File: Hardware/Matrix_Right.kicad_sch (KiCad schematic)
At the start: 0 parts

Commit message: Schematic review
Initial shcematic iteration.
Added all footprints and part numbers.
Only a quick review was performed.
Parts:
- added C48, C49, C50, C51, C52, C53, C54, C55, C56, C57, C58, C59, C60, C61, C62, C63, C64, C65, C66, C67, C68, C69, C70, C71, C72, C73, C74, C75, C76, C77, C78, C79, C80, C81, C82: 1u, Capacitor_SMD:C_0603_1608Metric, symbol Device:C
- added D100, D101, D107, D108, D109, D110, D111, D117, D118, D120, D121, D122, D127, D128, D130, D131, D132, D137, D138, D139, D140, D141, D77, D78, D79, D80, D81, D87, D88, D89, D90, D91, D97, D98, D99: SK6812MINI-E, LED_SMD:LED_SK6812MINI-E_3.2x2.8mm_P1.5mm_ReverseMount, symbol LED:SK6812MINI-E
- added D102, D103, D104, D105, D106, D112, D113, D114, D115, D116, D119, D123, D124, D125, D126, D129, D133, D134, D135, D136, D142, D143, D144, D145, D146, D82, D83, D84, D85, D86, D92, D93, D94, D95, D96: 1N4148WT, Diode_SMD:D_SOD-523, symbol Diode:1N4148WT
- added SW36, SW37, SW38, SW39, SW40, SW41, SW42, SW43, SW44, SW45, SW46, SW47, SW48, SW49, SW50, SW51, SW52, SW53, SW54, SW55, SW56, SW57, SW58, SW59, SW60, SW61, SW62, SW63, SW64, SW65, SW66, SW67: PG1350, Custom_Parts:PG1350_1.00u_PCB, symbol Switch:SW_Push
- added SW68: ENCODER, Custom_Parts:ALPS_EC11J_ENCODER, symbol Device:RotaryEncoder_Switch_MP
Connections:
- new net: D124.2 (A), SW57.2
- new net: D135.2 (A), SW62.2
- new net: D125.2 (A), SW58.2
- new net: D84.2 (A), SW38.2
- new net: D113.2 (A), SW52.2
- new net: D80.4 (DOUT), D90.2 (DIN)
- new net: D100.2 (DIN), D90.4 (DOUT)
- new net: D122.4 (DOUT), D132.2 (DIN)
- new net: D132.4 (DOUT), D141.2 (DIN)
- new net: D86.2 (A), SW40.2
- new net: D78.2 (DIN), D88.4 (DOUT)
- new net: D78.4 (DOUT), D81.2 (DIN)
- new net: D106.2 (A), SW50.2
- new net: D144.2 (A), SW66.2
- new net: D100.4 (DOUT), D110.2 (DIN)
- new net: D110.4 (DOUT), D121.2 (DIN)
- new net: D142.2 (A), SW64.2
- new net: D131.4 (DOUT), D140.2 (DIN)
- new net: D138.2 (DIN), D140.4 (DOUT)
- new net: D93.2 (A), SW42.2
- new net: D107.2 (DIN), D117.4 (DOUT)
- new net: D107.4 (DOUT), D97.2 (DIN)
- new net: D88.2 (DIN), D98.4 (DOUT)
- new net: D136.2 (A), SW63.2
- new net: D96.2 (A), SW45.2
- new net: D134.2 (A), SW61.2
- new net: D109.4 (DOUT), D120.2 (DIN)
- new net: D120.4 (DOUT), D130.2 (DIN)
- new net: D83.2 (A), SW37.2
- new net: D114.2 (A), SW53.2
- new net: D123.2 (A), SW56.2
- new net: D116.2 (A), SW55.2
- new net: D143.2 (A), SW65.2
- new net: D108.4 (DOUT), D98.2 (DIN)
- new net: D101.2 (DIN), D91.4 (DOUT)
- new net: D101.4 (DOUT), D111.2 (DIN)
- new net: D89.4 (DOUT), D99.2 (DIN)
- new net: D109.2 (DIN), D99.4 (DOUT)
- new net: D95.2 (A), SW44.2
- new net: D111.4 (DOUT), D122.2 (DIN)
- new net: D127.2 (DIN), D137.4 (DOUT)
- new net: D117.2 (DIN), D127.4 (DOUT)
- new net: D121.4 (DOUT), D131.2 (DIN)
- new net: D82.2 (A), SW36.2
- new net: D130.4 (DOUT), D139.2 (DIN)
- new net: D104.2 (A), SW48.2
- new net: D105.2 (A), SW49.2
- new net: D145.2 (A), SW67.2
- new net: D126.2 (A), SW59.2
- new net: D103.2 (A), SW47.2
- new net: D128.2 (DIN), D138.4 (DOUT)
- new net: D118.2 (DIN), D128.4 (DOUT)
- new net: D108.2 (DIN), D118.4 (DOUT)
- new net: D102.2 (A), SW46.2
- new net: D77.2 (DIN), D87.4 (DOUT)
- new net: D77.4 (DOUT), D80.2 (DIN)
- new net: D81.4 (DOUT), D91.2 (DIN)
- new net: D85.2 (A), SW39.2
- new net: D94.2 (A), SW43.2
- new net: D133.2 (A), SW60.2
- new net: D115.2 (A), SW54.2
- new net: D87.2 (DIN), D97.4 (DOUT)
- new net: D112.2 (A), SW51.2
- new net: D79.4 (DOUT), D89.2 (DIN)
- new net: D137.2 (DIN), D139.4 (DOUT)
- new net: D92.2 (A), SW41.2
- new net 5VR: C48.1, C49.1, C50.1, C51.1, C52.1, C53.1, C54.1, C55.1, C56.1, C57.1, C58.1, C59.1, C60.1, C61.1, C62.1, C63.1, C64.1, C65.1, C66.1, C67.1, C68.1, C69.1, C70.1, C71.1, C72.1, C73.1, C74.1, C75.1, C76.1, C77.1, C78.1, C79.1, C80.1, C81.1, C82.1, D100.3 (VDD), D101.3 (VDD), D107.3 (VDD), D108.3 (VDD), D109.3 (VDD), D110.3 (VDD), D111.3 (VDD), D117.3 (VDD), D118.3 (VDD), D120.3 (VDD), D121.3 (VDD), D122.3 (VDD), D127.3 (VDD), D128.3 (VDD), D130.3 (VDD), D131.3 (VDD), D132.3 (VDD), D137.3 (VDD), D138.3 (VDD), D139.3 (VDD), D140.3 (VDD), D141.3 (VDD), D77.3 (VDD), D78.3 (VDD), D79.3 (VDD), D80.3 (VDD), D81.3 (VDD), D87.3 (VDD), D88.3 (VDD), D89.3 (VDD), D90.3 (VDD), D91.3 (VDD), D97.3 (VDD), D98.3 (VDD), D99.3 (VDD)
- new net COL1_R: SW36.1, SW37.1, SW38.1, SW39.1, SW40.1
- new net COL2_R: SW41.1, SW42.1, SW43.1, SW44.1, SW45.1
- new net COL3_R: SW46.1, SW47.1, SW48.1, SW49.1, SW50.1
- new net COL4_R: SW51.1, SW52.1, SW53.1, SW54.1, SW55.1
- new net COL5_R: D119.2 (A), SW56.1, SW57.1, SW58.1, SW59.1
- new net COL6_R: D129.2 (A), SW60.1, SW61.1, SW62.1, SW63.1
- new net COL7_R: SW64.1, SW65.1, SW66.1, SW67.1, SW68.S1
- new net ENC_CC: D129.1 (K), SW68.B
- new net ENC_CW: D119.1 (K), SW68.A
- new net ENC_SW: D146.2 (A), SW68.S2
- new net GND: C48.2, C49.2, C50.2, C51.2, C52.2, C53.2, C54.2, C55.2, C56.2, C57.2, C58.2, C59.2, C60.2, C61.2, C62.2, C63.2, C64.2, C65.2, C66.2, C67.2, C68.2, C69.2, C70.2, C71.2, C72.2, C73.2, C74.2, C75.2, C76.2, C77.2, C78.2, C79.2, C80.2, C81.2, C82.2, D100.1 (VSS), D101.1 (VSS), D107.1 (VSS), D108.1 (VSS), D109.1 (VSS), D110.1 (VSS), D111.1 (VSS), D117.1 (VSS), D118.1 (VSS), D120.1 (VSS), D121.1 (VSS), D122.1 (VSS), D127.1 (VSS), D128.1 (VSS), D130.1 (VSS), D131.1 (VSS), D132.1 (VSS), D137.1 (VSS), D138.1 (VSS), D139.1 (VSS), D140.1 (VSS), D141.1 (VSS), D77.1 (VSS), D78.1 (VSS), D79.1 (VSS), D80.1 (VSS), D81.1 (VSS), D87.1 (VSS), D88.1 (VSS), D89.1 (VSS), D90.1 (VSS), D91.1 (VSS), D97.1 (VSS), D98.1 (VSS), D99.1 (VSS), SW68.MP
- new net LED_DATA_R: D79.2 (DIN)
- new net ROW1_R: D102.1 (K), D112.1 (K), D123.1 (K), D133.1 (K), D142.1 (K), D82.1 (K), D92.1 (K)
- new net ROW2_R: D103.1 (K), D113.1 (K), D124.1 (K), D134.1 (K), D143.1 (K), D83.1 (K), D93.1 (K)
- new net ROW3_R: D104.1 (K), D114.1 (K), D125.1 (K), D135.1 (K), D144.1 (K), D84.1 (K), D94.1 (K)
- new net ROW4_R: D105.1 (K), D115.1 (K), D126.1 (K), D136.1 (K), D145.1 (K), D85.1 (K), D95.1 (K)
- new net ROW5_R: D106.1 (K), D116.1 (K), D146.1 (K), D86.1 (K), D96.1 (K), SW68.C
- no-connect marks 0 -> 1

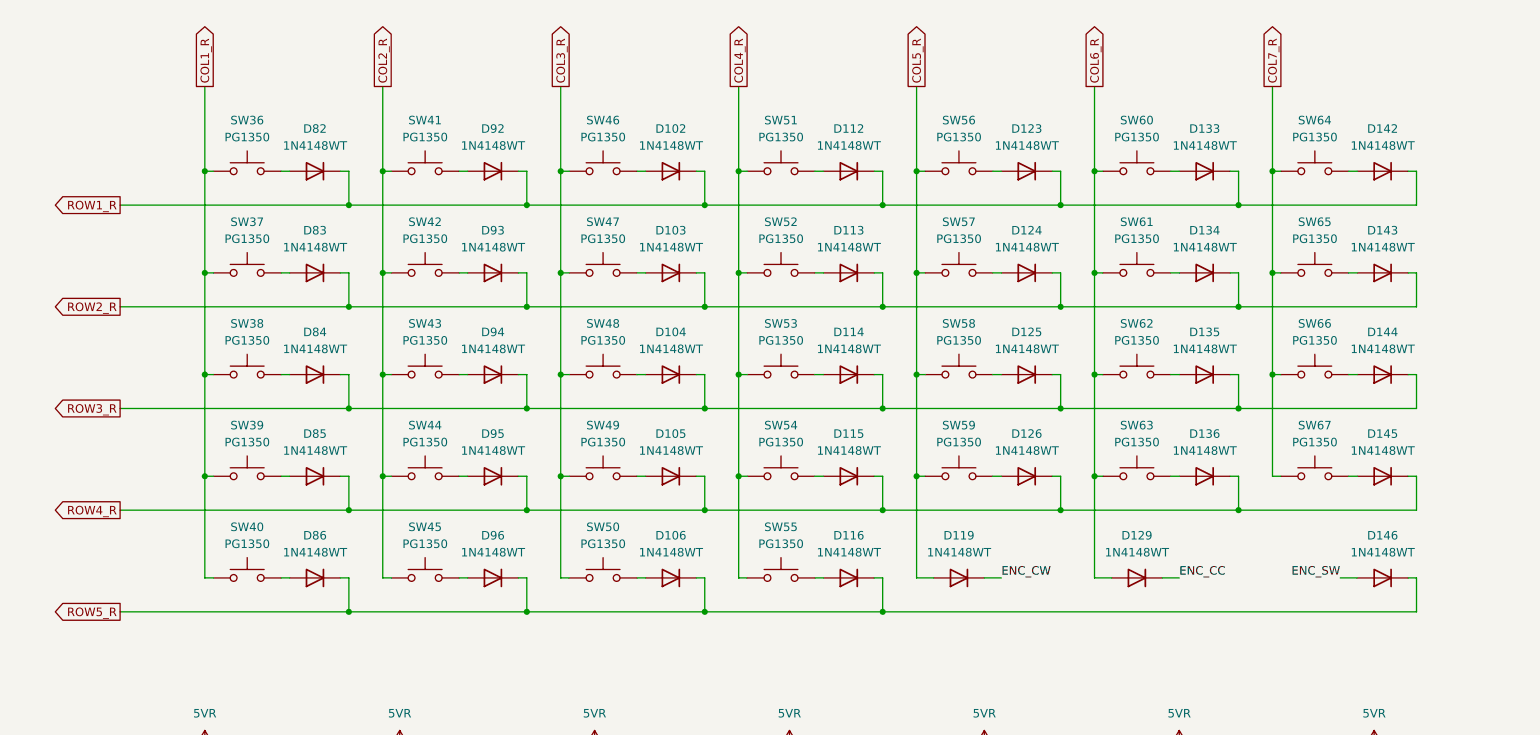
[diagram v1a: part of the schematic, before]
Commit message: Net configurations
Added net labels.
Updated the PCB components.
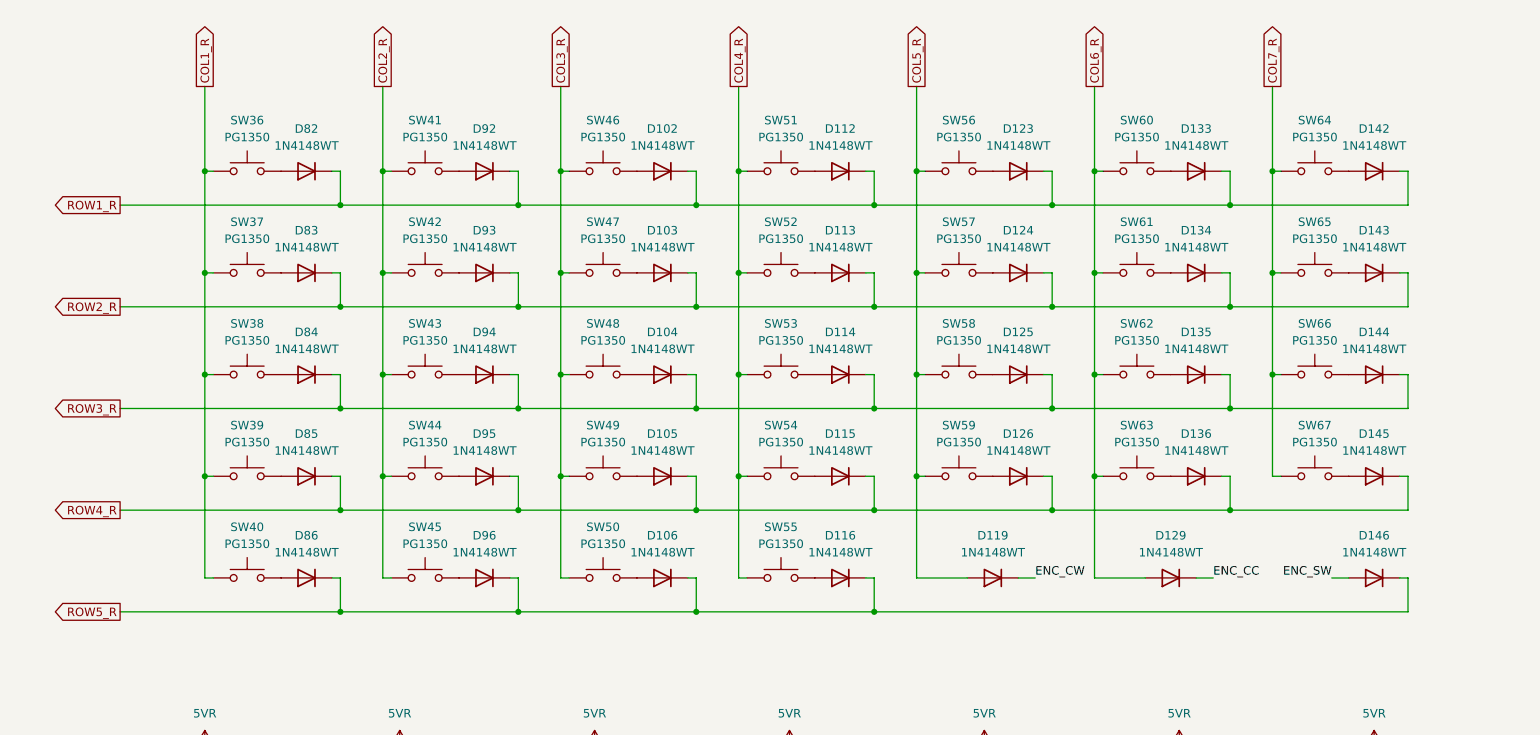
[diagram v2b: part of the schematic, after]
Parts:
- D100, D101, D107, D108, D109, D110, D111, D117, D118, D120, D121, D122, D127, D128, D130, D131, D132, D137, D138, D139, D140, D141, D77, D78, D79, D80, D81, D87, D88, D89, D90, D91, D97, D98, D99: footprint LED_SMD:LED_SK6812MINI-E_3.2x2.8mm_P1.5mm_ReverseMount -> Custom_Parts:LED_SK6812MINI-E_3.2x2.8mm_P1.5mm_ReverseMount
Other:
- moved on the sheet: D102, D103, D104, D105, D106, D112, D113, D114, D115, D116, D119, D123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

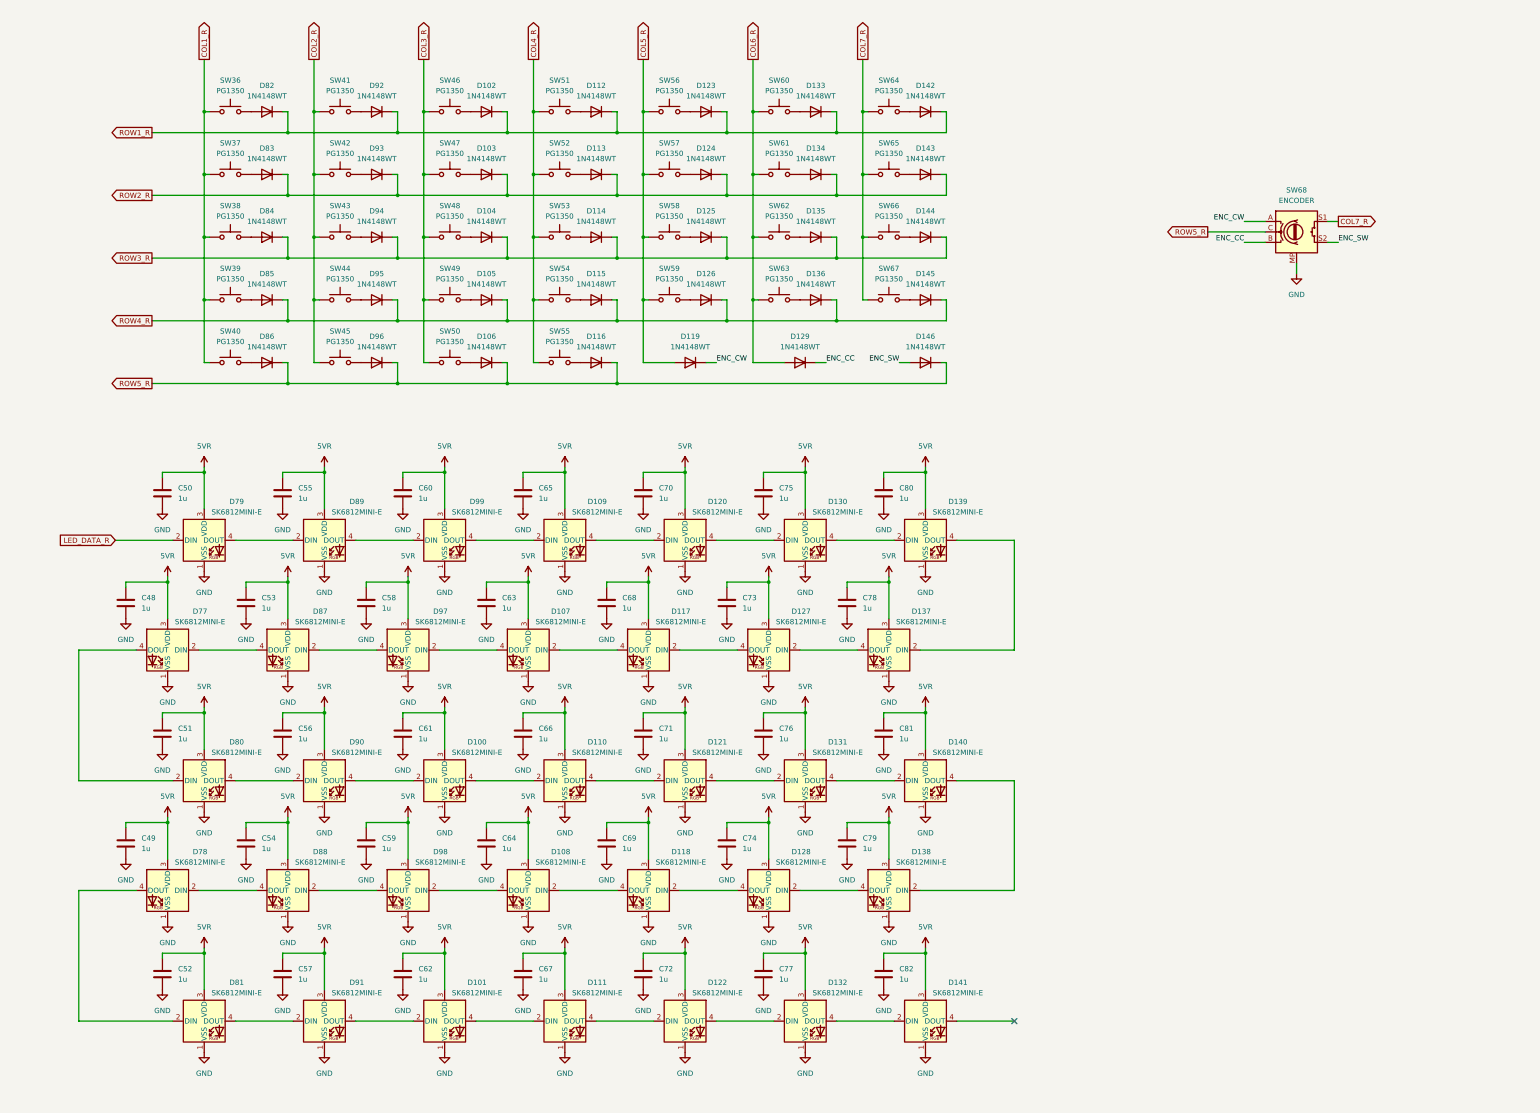
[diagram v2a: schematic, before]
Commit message: Initial layout
Configured the switch and LED initial layout.
Need to add the capacitors for the LEDs and the diodes for the switches.
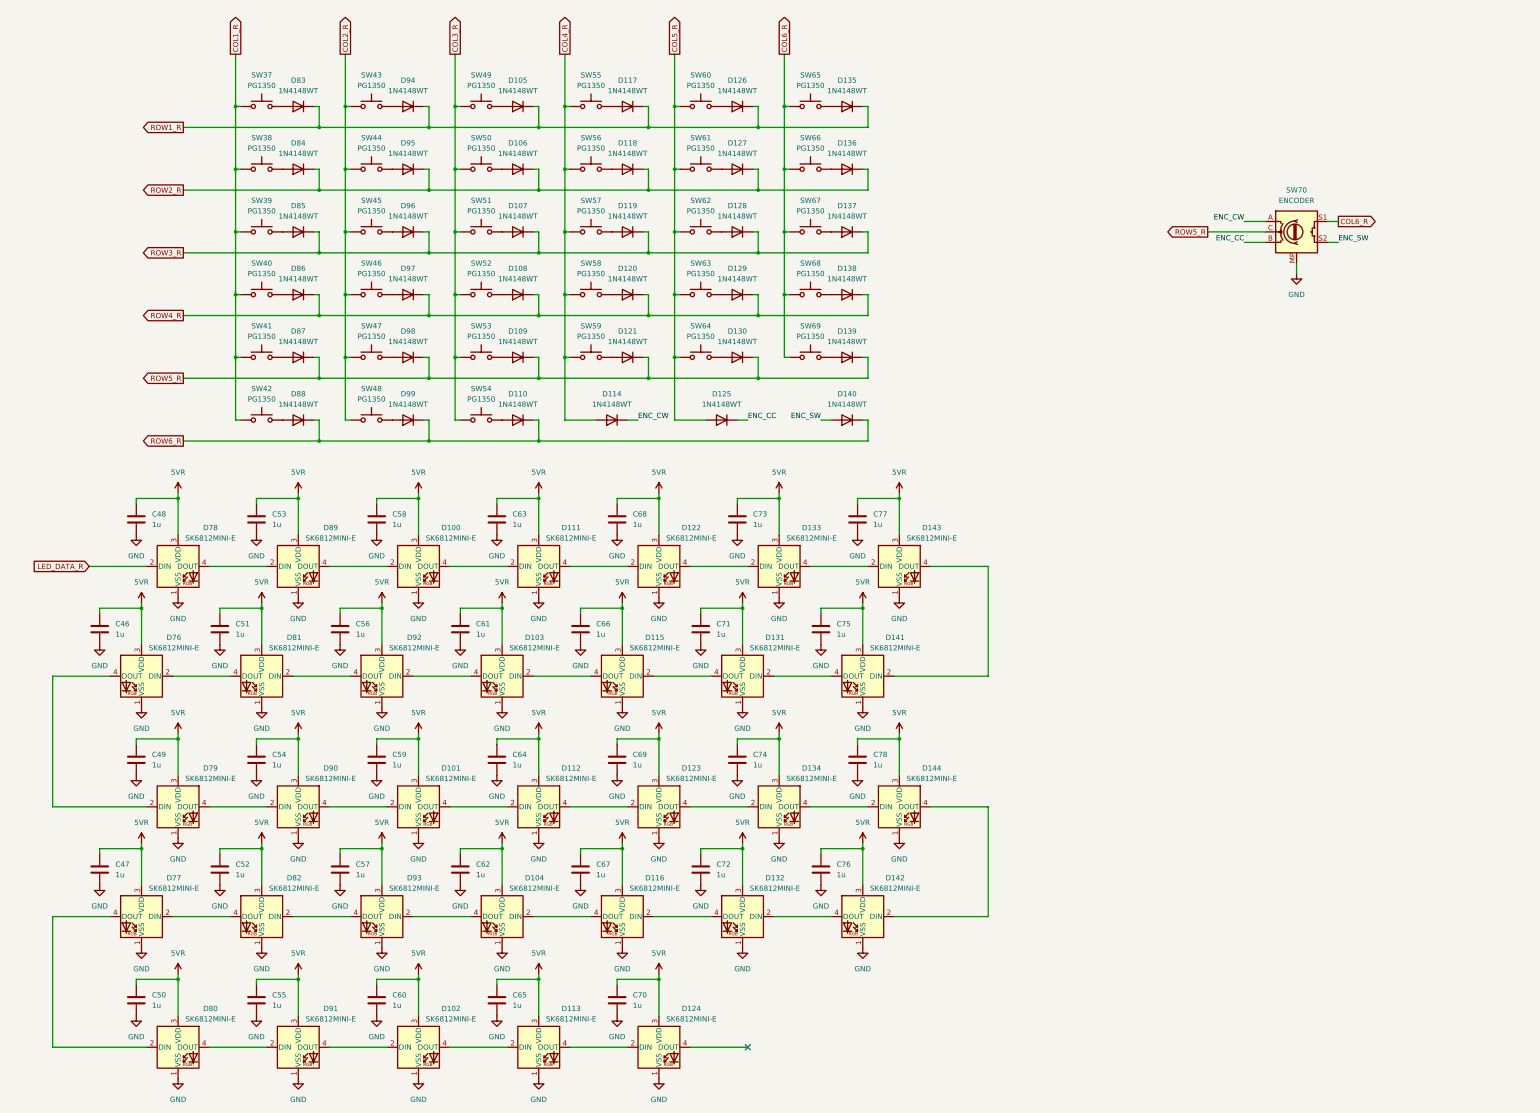
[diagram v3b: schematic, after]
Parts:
- removed C77, C82: 1u, Capacitor_SMD:C_0603_1608Metric, symbol Device:C
- removed D102, D103, D104, D112, D113, D115, D116, D123, D124, D133, D134, D142, D143, D144, D145, D146, D82, D92, D93: 1N4148WT, Diode_SMD:D_SOD-523, symbol Diode:1N4148WT
- removed D132, D141: SK6812MINI-E, Custom_Parts:LED_SK6812MINI-E_3.2x2.8mm_P1.5mm_ReverseMount, symbol LED:SK6812MINI-E
- removed SW36: PG1350, Custom_Parts:PG1350_1.00u_PCB, symbol Switch:SW_Push
- added D107, D108, D109, D110, D117, D118, D120, D121, D127, D128, D130, D137, D138, D139, D140, D87, D88, D97, D98, D99: 1N4148WT, Diode_SMD:D_SOD-523, symbol Diode:1N4148WT
- added SW68, SW69: PG1350, Custom_Parts:PG1350_1.00u_PCB, symbol Switch:SW_Push
- renumbered C48 to C46, C49 to C47, C50 to C48, C51 to C49, C52 to C50, C53 to C51, C54 to C52, C55 to C53, C56 to C54, C57 to C55, C58 to C56, C59 to C57, C60 to C58, C61 to C59, C62 to C60, C63 to C61, C64 to C62, C65 to C63, C66 to C64, C67 to C65, C68 to C66, C69 to C67, C70 to C68, C71 to C69, C72 to C70, C73 to C71, C74 to C72, C75 to C73, C76 to C74, C78 to C75, C79 to C76, C80 to C77, C81 to C78, D99 to D100, D100 to D101, D101 to D102, D107 to D103, D108 to D104, D109 to D111, D110 to D112, D111 to D113, D117 to D115, D118 to D116, D120 to D122, D121 to D123, D122 to D124, D127 to D131, D128 to D132, D130 to D133, D131 to D134, D137 to D141, D138 to D142, D139 to D143, D140 to D144, D77 to D76, D78 to D77, D79 to D78, D80 to D79, D81 to D80, D87 to D81, D88 to D82, D97 to D92, D98 to D93, SW68 to SW70
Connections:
- net COL1_R: now also SW41.1, SW42.1
- net COL2_R: now also SW46.1, SW47.1, SW48.1; no longer SW41.1, SW42.1
- net COL3_R: now also SW51.1, SW52.1, SW53.1, SW54.1; no longer SW46.1, SW47.1, SW48.1
- net COL4_R: now also D114.2 (A), SW56.1, SW57.1, SW58.1, SW59.1; no longer SW51.1, SW52.1, SW53.1, SW54.1
- net COL5_R: now also D125.2 (A), SW60.1, SW61.1, SW62.1, SW63.1, SW64.1; no longer D119.2 (A), SW56.1, SW57.1, SW58.1, SW59.1
- net COL6_R: now also SW65.1, SW66.1, SW67.1, SW70.S1, SW68.1, SW69.1; no longer D129.2 (A), SW60.1, SW61.1, SW62.1, SW63.1
- net ENC_CC: now also D125.1 (K); no longer D129.1 (K)
- net ENC_CW: now also D114.1 (K); no longer D119.1 (K)
- net ENC_SW: now also D140.2 (A)
- net ROW1_R: now also D105.1 (K), D126.1 (K), D135.1 (K), D83.1 (K), D94.1 (K), D117.1 (K)
- net ROW2_R: now also D106.1 (K), D136.1 (K), D84.1 (K), D95.1 (K), D118.1 (K), D127.1 (K); no longer D83.1 (K)
- net ROW3_R: now also D119.1 (K), D85.1 (K), D96.1 (K), D107.1 (K), D128.1 (K), D137.1 (K); no longer D114.1 (K), D125.1 (K), D135.1 (K), D84.1 (K), D94.1 (K)
- net ROW4_R: now also D129.1 (K), D86.1 (K), D108.1 (K), D120.1 (K), D138.1 (K), D97.1 (K); no longer D105.1 (K), D126.1 (K), D136.1 (K), D85.1 (K), D95.1 (K)
- net ROW5_R: now also D109.1 (K), D121.1 (K), D130.1 (K), D139.1 (K), D87.1 (K), D98.1 (K); no longer D106.1 (K), D86.1 (K), D96.1 (K)
- net at SW57.2: now also D119.2 (A)
- net at D135.2 (A): now also SW65.2; no longer SW62.2
- net at SW58.2: now also D120.2 (A); no longer D125.2 (A)
- net at SW52.2: now also D108.2 (A)
- net at SW66.2: now also D136.2 (A)
- net at SW64.2: now also D130.2 (A)
- net at SW42.2: now also D88.2 (A)
- net at SW63.2: now also D129.2 (A); no longer D136.2 (A)
- net at SW61.2: now also D127.2 (A)
- net at SW53.2: now also D109.2 (A); no longer D114.2 (A)
- net at SW56.2: now also D118.2 (A)
- net at SW55.2: now also D117.2 (A)
- net at SW48.2: now also D99.2 (A)
- net at SW67.2: now also D137.2 (A)
- net at D126.2 (A): now also SW60.2; no longer SW59.2
- net at SW47.2: now also D98.2 (A)
- net at SW46.2: now also D97.2 (A)
- net at SW54.2: now also D110.2 (A)
- net at SW51.2: now also D107.2 (A)
- net at SW41.2: now also D87.2 (A)
- removed net COL7_R: SW64.1, SW65.1, SW66.1, SW67.1, SW70.S1
- new net: D138.2 (A), SW68.2
- new net: D139.2 (A), SW69.2
- new net: D128.2 (A), SW62.2
- new net: D121.2 (A), SW59.2
- new net ROW6_R: D110.1 (K), D140.1 (K), D88.1 (K), D99.1 (K)
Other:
- moved on the sheet: C46, C47, C48, C49, C50, C51, C52, C53, C54, C55, C56, C57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
